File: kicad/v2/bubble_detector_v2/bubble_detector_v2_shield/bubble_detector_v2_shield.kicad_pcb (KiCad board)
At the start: 2 copper layers, 68.6 x 53.3 mm, 9 parts, among them J1 Power, J2 Digital/PWM, J3 Analog, J4 Digital/PWM, U1 HC-SR04

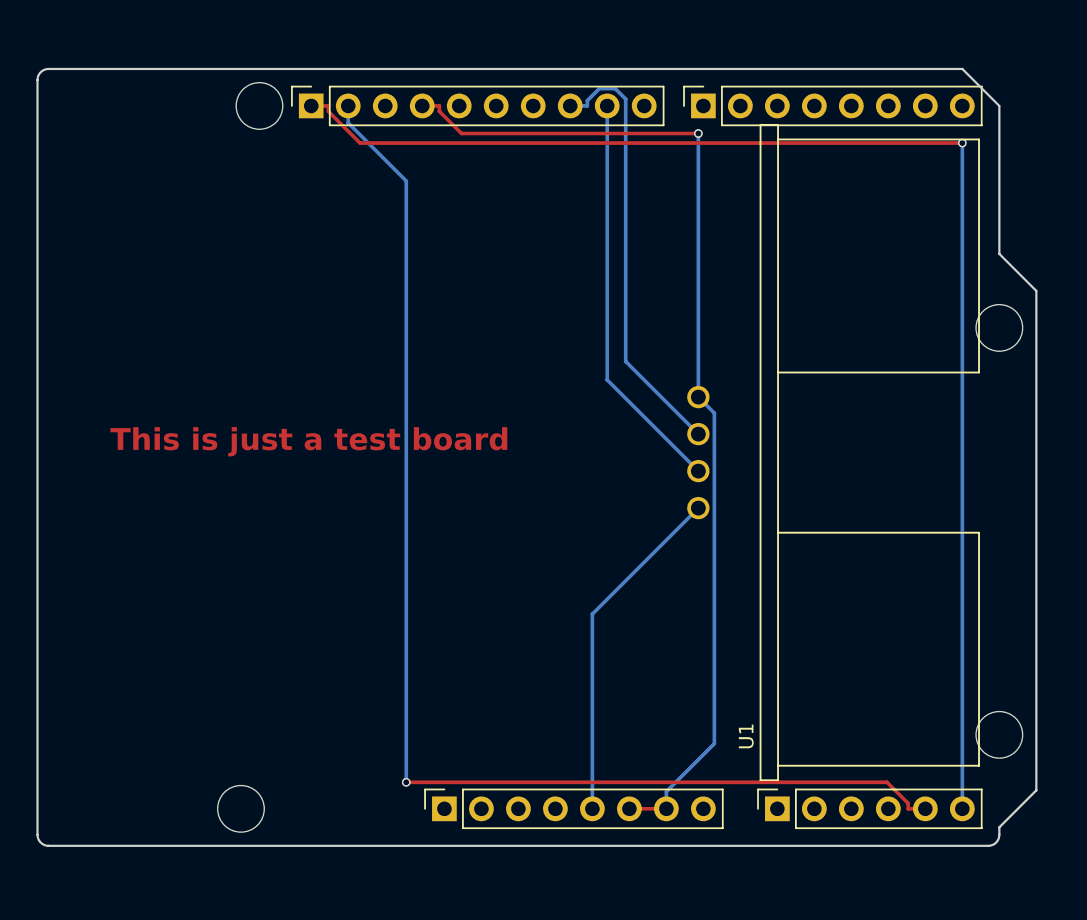
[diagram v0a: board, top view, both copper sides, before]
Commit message: missing edge cut
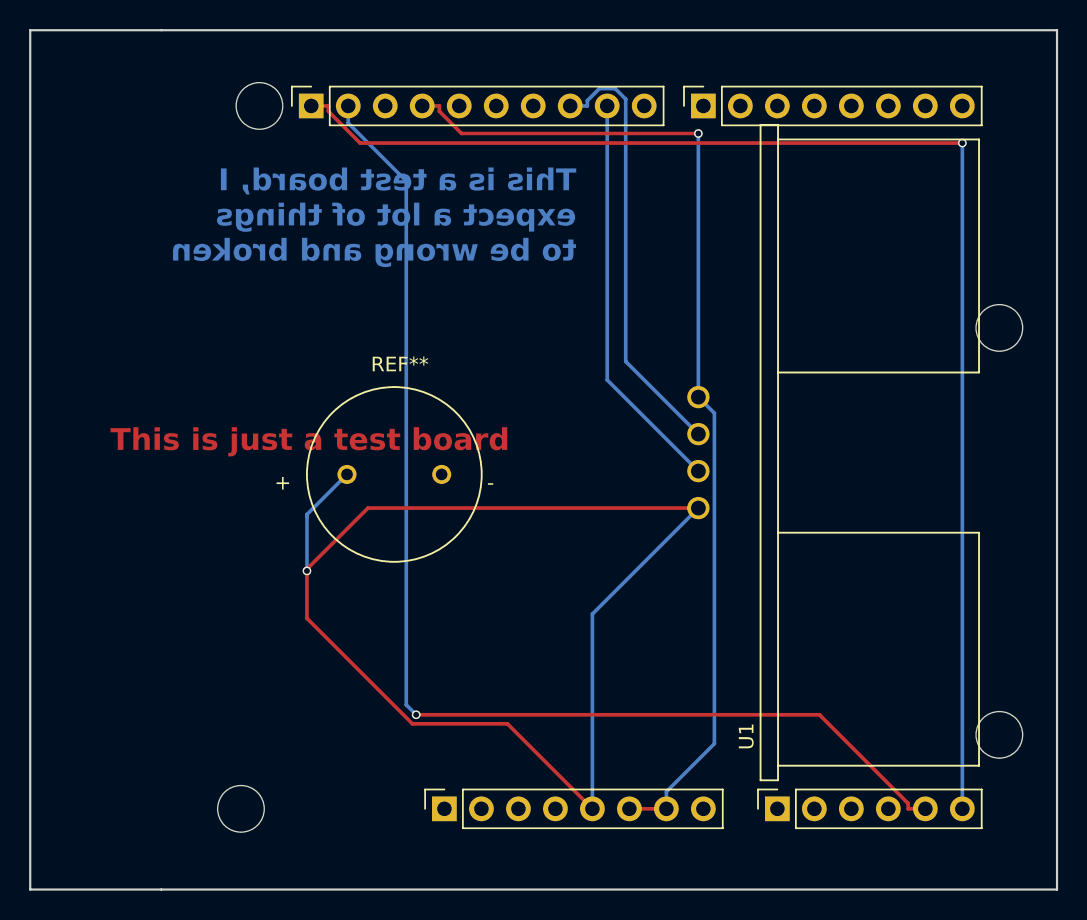
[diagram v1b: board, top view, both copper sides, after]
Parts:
- added REF**: CUI_CEM-1203_42_, Speaker_CEM-1203_42:CUI_CEM-1203_42_, F.Cu at (124.5, 74.5)
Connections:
- J1 pad 5: +5V -> (no net)
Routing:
- net +5V: track 23.7 -> 88.8 mm, vias 0 -> 1
- net /SDA/A4: track 84.7 -> 81.6 mm
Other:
- board size 68.6 x 53.3 mm -> 70.5 x 59 mm
- board text added: "This is a test board, I expect a lot of things to be wrong and broken"
